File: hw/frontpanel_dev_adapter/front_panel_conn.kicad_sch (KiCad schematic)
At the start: 18 parts, among them J301 FFC_conn_14p, J302 FFC_conn_14p, J303 JST_S2B-PH-SM4-TB, J304 Conn_01x02, Q301 AO3400A, U301 TLV9051SIDBV

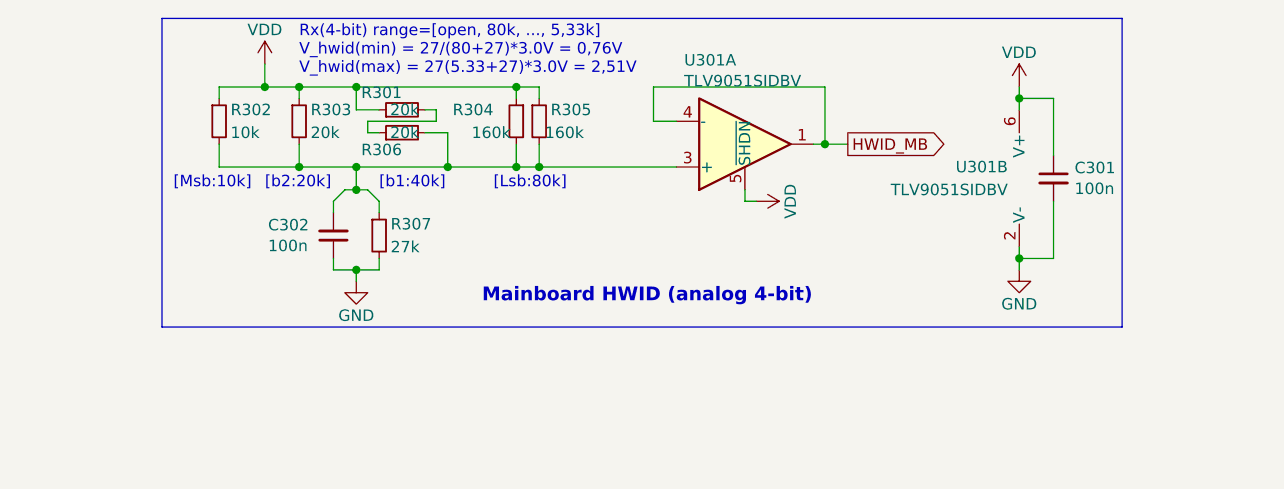
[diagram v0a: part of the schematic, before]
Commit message: Various boards & schematics (auto-)updated to Kicad-v8
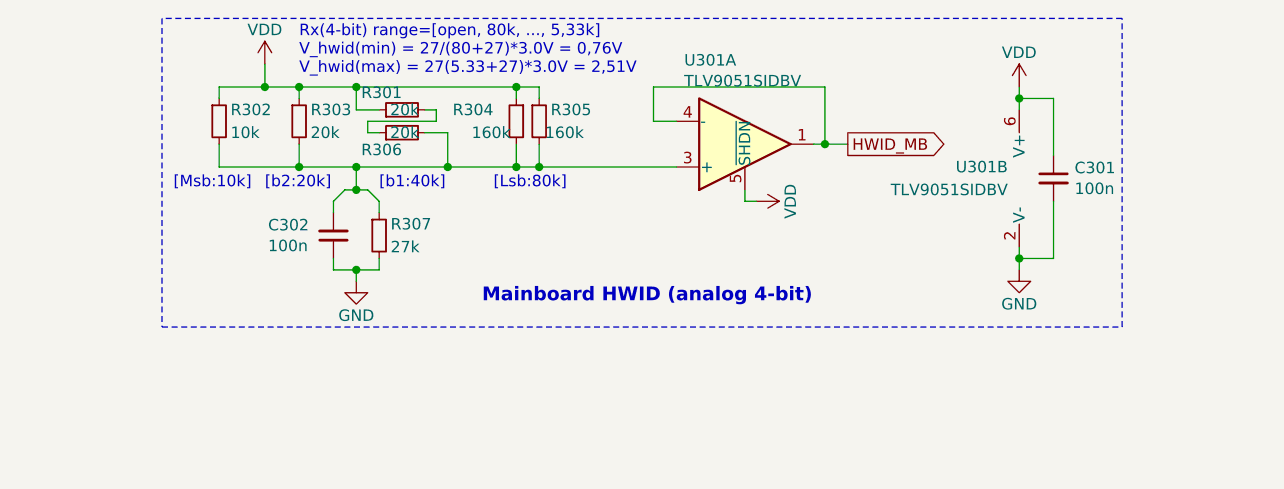
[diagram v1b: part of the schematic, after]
